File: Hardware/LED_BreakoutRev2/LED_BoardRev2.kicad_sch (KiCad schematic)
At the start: 33 parts, among them Q1 BSS214NW, Q2 BSS214NW, Q3 BSS214NW, Q4 BSS214NW, Q5 BSS214NW, Q6 BSS214NW

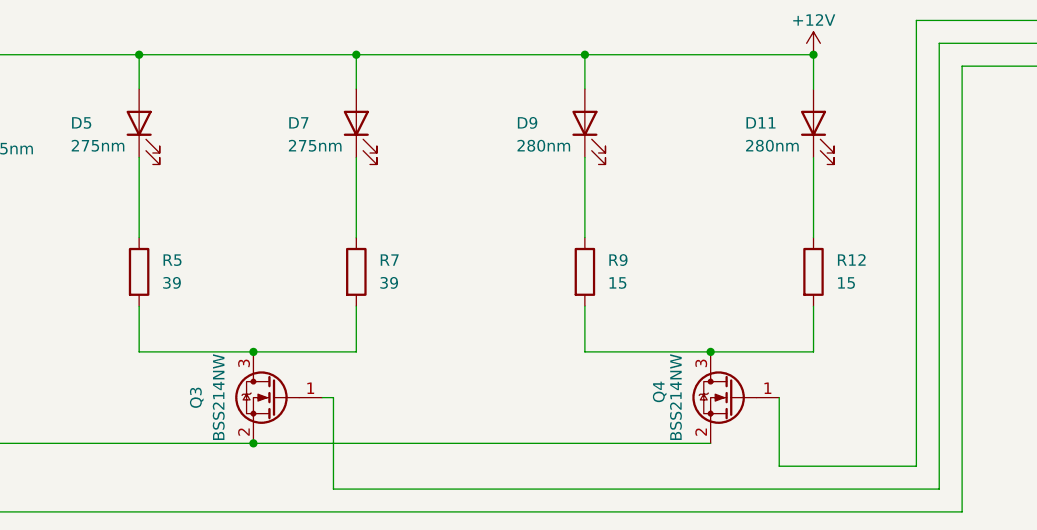
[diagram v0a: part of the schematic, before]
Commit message: Fixed resistor values
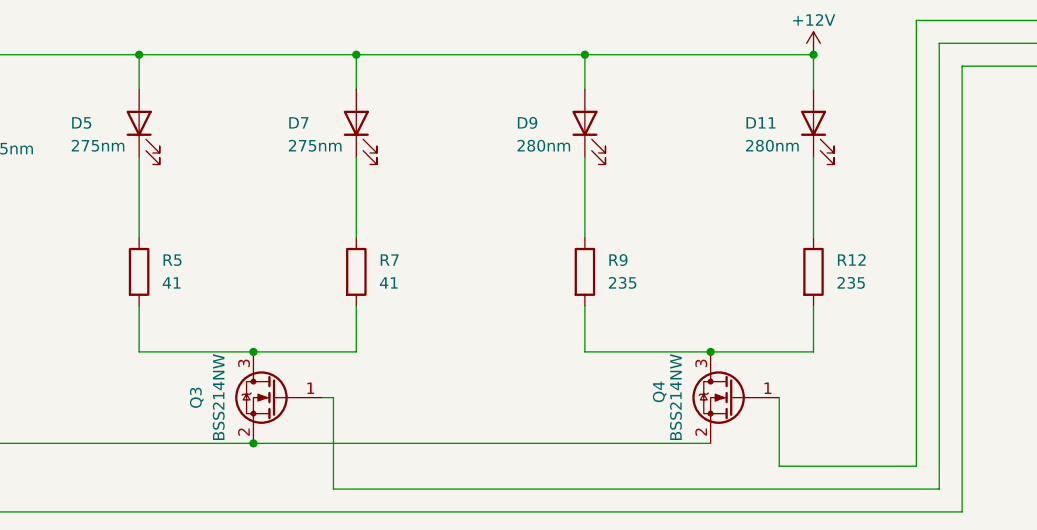
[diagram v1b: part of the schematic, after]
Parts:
- R12, R9: value 15 -> 235
- R5, R7: value 39 -> 41
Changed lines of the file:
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@@
       (effects (font (size 1.27 1.27)) (justify left))
     )
-    (property "Value" "15" (id 1) (at 201.93 110.4899 0)
+    (property "Value" "235" (id 1) (at 201.93 110.4899 0)
       (effects (font (size 1.27 1.27)) (justify left))
     )
@@
       (effects (font (size 1.27 1.27)) hide)
     )
-    (property "Datasheet" "https://www.digikey.com/en/products/detail/te-connectivity-passive-product/352215RFT/5244998" (id 3) (at 199.39 109.22 0)
+    (property "Datasheet" "https://www.mouser.com/ProductDetail/YAGEO/RT1206BRC07250RL?qs=sGAEpiMZZMtlubZbdhIBINSnPd898yDPjn3BpsSGDUg%3D" (id 3) (at 199.39 109.22 0)
       (effects (font (size 1.27 1.27)) hide)
     )
@@
       (effects (font (size 1.27 1.27)) (justify left))
     )
-    (property "Value" "39" (id 1) (at 151.13 110.4899 0)
+    (property "Value" "41" (id 1) (at 151.13 110.4899 0)
       (effects (font (size 1.27 1.27)) (justify left))
     )
@@
       (effects (font (size 1.27 1.27)) (justify left))
     )
-    (property "Value" "15" (id 1) (at 176.53 110.4899 0)
+    (property "Value" "235" (id 1) (at 176.53 110.4899 0)
       (effects (font (size 1.27 1.27)) (justify left))
     )
@@
       (effects (font (size 1.27 1.27)) hide)
     )
-    (property "Datasheet" "https://www.digikey.com/en/products/detail/te-connectivity-passive-product/352215RFT/5244998" (id 3) (at 173.99 109.22 0)
+    (property "Datasheet" "https://www.mouser.com/ProductDetail/YAGEO/RT1206BRC07250RL?qs=sGAEpiMZZMtlubZbdhIBINSnPd898yDPjn3BpsSGDUg%3D" (id 3) (at 173.99 109.22 0)
       (effects (font (size 1.27 1.27)) hide)
     )
@@
       (effects (font (size 1.27 1.27)) (justify left))
     )
-    (property "Value" "39" (id 1) (at 127 110.4899 0)
+    (property "Value" "41" (id 1) (at 127 110.4899 0)
       (effects (font (size 1.27 1.27)) (justify left))
     )
@@
     )
     (path "/93e48d0b-eba6-4854-bc8a-17e527f014a3"
-      (reference "R5") (unit 1) (value "39") (footprint "Resistor_SMD:R_2512_6332Metric_Pad1.40x3.35mm_HandSolder")
+      (reference "R5") (unit 1) (value "41") (footprint "Resistor_SMD:R_2512_6332Metric_Pad1.40x3.35mm_HandSolder")
     )
     (path "/d17db897-84e6-4022-9dc4-4eecd630bc5e"
@@
     )
     (path "/240d6f4d-65b2-4461-b47d-786ff4cb3d7c"
-      (reference "R7") (unit 1) (value "39") (footprint "Resistor_SMD:R_2512_6332Metric_Pad1.40x3.35mm_HandSolder")
+      (reference "R7") (unit 1) (value "41") (footprint "Resistor_SMD:R_2512_6332Metric_Pad1.40x3.35mm_HandSolder")
     )
     (path "/1e5baa22-f800-4ee7-823e-07c8c8a82f1b"
@@
     )
     (path "/4640cc32-5742-46fb-92d3-8c957470f387"
-      (reference "R9") (unit 1) (value "15") (footprint "Resistor_SMD:R_2512_6332Metric_Pad1.40x3.35mm_HandSolder")
+      (reference "R9") (unit 1) (value "235") (footprint "Resistor_SMD:R_2512_6332Metric_Pad1.40x3.35mm_HandSolder")
     )
     (path "/7d784730-35d8-402c-a5c8-e39754989647"
@@
     )
     (path "/1d427fac-f5cd-4da2-9ce4-13d315414bcf"
-      (reference "R12") (unit 1) (value "15") (footprint "Resistor_SMD:R_2512_6332Metric_Pad1.40x3.35mm_HandSolder")
+      (reference "R12") (unit 1) (value "235") (footprint "Resistor_SMD:R_2512_6332Metric_Pad1.40x3.35mm_HandSolder")
     )
     (path "/fc7a2316-8b3d-43bf-ad9b-b37462b729ed"

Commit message: Update datasheet
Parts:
- removed R10, R11, R13: 4, MRDT_Devices:Stupid 4 Ohm Resistor, symbol Device:R
- removed R12: 235, Resistor_SMD:R_2512_6332Metric_Pad1.40x3.35mm_HandSolder, symbol Device:R
- added R?: 16, MRDT_Devices:Stupid 4 Ohm Resistor, symbol Device:R
- added R?: 237, Resistor_SMD:R_2512_6332Metric_Pad1.40x3.35mm_HandSolder, symbol Device:R
- R1: value 250 -> 325
- R14: value 4 -> 16
- R4, R6, R8: value 150 -> 325
- R5, R7: value 41 -> 39
- R9: value 235 -> 237
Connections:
- net at D10.1 (K): now also R?.1
- net at D11.1 (K): now also R?.1
- net at Q4.3 (D), R9.2: now also R?.2
- net at D12.1 (K): now also R14.1
- net at Q5.3 (D), Q6.3 (D), R14.2: now also R?.2
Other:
- moved on the sheet: R14

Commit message: Concept LED layout
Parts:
- removed R14: 16, MRDT_Devices:Stupid 4 Ohm Resistor, symbol Device:R
- added R12: 16, Resistor_SMD:R_2512_6332Metric_Pad1.40x3.35mm_HandSolder, symbol Device:R
- R10: renamed from R?; footprint MRDT_Devices:Stupid 4 Ohm Resistor -> Resistor_SMD:R_2512_6332Metric_Pad1.40x3.35mm_HandSolder
- gave numbers to parts that had none: 1
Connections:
- net at Q5.3 (D), Q6.3 (D), R10.2: now also R12.2
- net at D12.1 (K): now also R12.1
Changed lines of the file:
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@@
   (symbol (lib_id "Device:R") (at 190.5 52.07 0) (unit 1)
     (in_bom yes) (on_board yes) (fields_autoplaced)
-    (property "Reference" "R?" (id 0) (at 193.04 50.7999 0)
+    (property "Reference" "R10" (id 0) (at 193.04 50.7999 0)
       (effects (font (size 1.27 1.27)) (justify left))
     )
@@
       (effects (font (size 1.27 1.27)) (justify left))
     )
-    (property "Footprint" "MRDT_Devices:Stupid 4 Ohm Resistor" (id 2) (at 188.722 52.07 90)
+    (property "Footprint" "Resistor_SMD:R_2512_6332Metric_Pad1.40x3.35mm_HandSolder" (id 2) (at 188.722 52.07 90)
       (effects (font (size 1.27 1.27)) hide)
     )
@@
     (pin "2")
   )
+  (symbol (lib_id "Device:R") (at 209.55 52.07 0) (unit 1)
+    (in_bom yes) (on_board yes) (fields_autoplaced)
+    (property "Reference" "R12" (id 0) (at 212.09 50.7999 0)
+      (effects (font (size 1.27 1.27)) (justify left))
+    )
+    (property "Value" "16" (id 1) (at 212.09 53.3399 0)
+      (effects (font (size 1.27 1.27)) (justify left))
+    )
+    (property "Footprint" "Resistor_SMD:R_2512_6332Metric_Pad1.40x3.35mm_HandSolder" (id 2) (at 207.772 52.07 90)
+      (effects (font (size 1.27 1.27)) hide)
+    )
+    (property "Datasheet" "https://www.digikey.com/en/products/detail/te-connectivity-passive-product/355016RFT/9927086?s=N4IgjCBcoExaBjKAzAhgGwM4FMA0IB7KAbRBgBYBOANgpAF18AHAFyhAGUWAnASwDsA5iAC%2B%2BAMzwQSSGix5CJcGHERGIVuy58ho-DAAMADgCsUmXJz4ikUmGoACAPIALALaYGzNpBABVfl4WJ2QAWWxUTABXbmw9EABaOGhpKB4ohRtSM3oRPKA" (id 3) (at 209.55 52.07 0)
+      (effects (font (size 1.27 1.27)) hide)
+    )
+    (pin "1")
+    (pin "2")
+  )
   (symbol (lib_id "Device:LED") (at 102.87 92.71 90) (unit 1)
     (in_bom yes) (on_board yes) (fields_autoplaced)
@@
     (pin "2")
   )
-  (symbol (lib_id "Device:R") (at 209.55 52.07 0) (unit 1)
-    (in_bom yes) (on_board yes) (fields_autoplaced)
-    (property "Reference" "R14" (id 0) (at 212.09 50.7999 0)
-      (effects (font (size 1.27 1.27)) (justify left))
-    )
-    (property "Value" "16" (id 1) (at 212.09 53.3399 0)
-      (effects (font (size 1.27 1.27)) (justify left))
-    )
-    (property "Footprint" "MRDT_Devices:Stupid 4 Ohm Resistor" (id 2) (at 207.772 52.07 90)
-      (effects (font (size 1.27 1.27)) hide)
-    )
-    (property "Datasheet" "https://www.digikey.com/en/products/detail/te-connectivity-passive-product/355016RFT/9927086?s=N4IgjCBcoExaBjKAzAhgGwM4FMA0IB7KAbRBgBYBOANgpAF18AHAFyhAGUWAnASwDsA5iAC%2B%2BAMzwQSSGix5CJcGHERGIVuy58ho-DAAMADgCsUmXJz4ikUmGoACAPIALALaYGzNpBABVfl4WJ2QAWWxUTABXbmw9EABaOGhpKB4ohRtSM3oRPKA" (id 3) (at 209.55 52.07 0)
-      (effects (font (size 1.27 1.27)) hide)
-    )
-    (pin "1")
-    (pin "2")
-  )
   (symbol (lib_id "Device:R") (at 134.62 50.8 0) (unit 1)
     (in_bom yes) (on_board yes) (fields_autoplaced)
@@
   (symbol (lib_id "Device:R") (at 199.39 109.22 0) (unit 1)
     (in_bom yes) (on_board yes) (fields_autoplaced)
-    (property "Reference" "R?" (id 0) (at 201.93 107.9499 0)
+    (property "Reference" "R11" (id 0) (at 201.93 107.9499 0)
       (effects (font (size 1.27 1.27)) (justify left))
     )
@@
       (reference "R9") (unit 1) (value "237") (footprint "Resistor_SMD:R_2512_6332Metric_Pad1.40x3.35mm_HandSolder")
     )
-    (path "/c5a7d028-8d34-4c0f-a3a9-dcd478aff00e"
-      (reference "R14") (unit 1) (value "16") (footprint "MRDT_Devices:Stupid 4 Ohm Resistor")
-    )
     (path "/2554a1ee-c9a5-4022-9b27-f04f246a3a90"
-      (reference "R?") (unit 1) (value "16") (footprint "MRDT_Devices:Stupid 4 Ohm Resistor")
+      (reference "R10") (unit 1) (value "16") (footprint "Resistor_SMD:R_2512_6332Metric_Pad1.40x3.35mm_HandSolder")
     )
     (path "/d92f54a0-29d1-4247-85fa-7317112c0582"
-      (reference "R?") (unit 1) (value "237") (footprint "Resistor_SMD:R_2512_6332Metric_Pad1.40x3.35mm_HandSolder")
-    )
-  )
+      (reference "R11") (unit 1) (value "237") (footprint "Resistor_SMD:R_2512_6332Metric_Pad1.40x3.35mm_HandSolder")
+    )
+    (path "/4e94a3e2-c33c-4c00-83d6-277a72b6be7a"
+      (reference "R12") (unit 1) (value "16") (footprint "Resistor_SMD:R_2512_6332Metric_Pad1.40x3.35mm_HandSolder")
+    )
+  )

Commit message: Still moving footprints
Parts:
- D5, D7: footprint MRDT_Devices:275nm LED -> Footprints:SU CULCN1.VC
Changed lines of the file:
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@@
-    (pin "2")
-  )
-  (symbol (lib_id "Device:LED") (at 148.59 92.71 90) (unit 1)
-    (in_bom yes) (on_board yes)
-    (property "Reference" "D7" (id 0) (at 140.97 92.71 90)
-      (effects (font (size 1.27 1.27)) (justify right))
-    )
-    (property "Value" "275nm" (id 1) (at 140.97 95.25 90)
-      (effects (font (size 1.27 1.27)) (justify right))
-    )
-    (property "Footprint" "MRDT_Devices:275nm LED" (id 2) (at 148.59 92.71 0)
-      (effects (font (size 1.27 1.27)) hide)
-    )
-    (property "Datasheet" "https://www.mouser.com/ProductDetail/ams-OSRAM/SU-CULCN1VC-GAGD-67-0-100-R18?qs=QNEnbhJQKvYzTEg60TYLDA%3D%3D&mgh=1&gclid=Cj0KCQjww4-hBhCtARIsAC9gR3Yx9EYuuzoX6Epv-96pbTp_j3rO-uPwrYGY7enRByVU-IZeXYdc4EkaAnjkEALw_wcB" (id 3) (at 148.59 92.71 0)
-      (effects (font (size 1.27 1.27)) hide)
-    )
-    (pin "1")
     (pin "2")
   )
@@
     (pin "1")
   )
+  (symbol (lib_id "Device:LED") (at 148.59 92.71 90) (unit 1)
+    (in_bom yes) (on_board yes)
+    (property "Reference" "D7" (id 0) (at 140.97 92.71 90)
+      (effects (font (size 1.27 1.27)) (justify right))
+    )
+    (property "Value" "275nm" (id 1) (at 140.97 95.25 90)
+      (effects (font (size 1.27 1.27)) (justify right))
+    )
+    (property "Footprint" "Footprints:SU CULCN1.VC" (id 2) (at 148.59 92.71 0)
+      (effects (font (size 1.27 1.27)) hide)
+    )
+    (property "Datasheet" "https://www.mouser.com/ProductDetail/ams-OSRAM/SU-CULCN1VC-GAGD-67-0-100-R18?qs=QNEnbhJQKvYzTEg60TYLDA%3D%3D&mgh=1&gclid=Cj0KCQjww4-hBhCtARIsAC9gR3Yx9EYuuzoX6Epv-96pbTp_j3rO-uPwrYGY7enRByVU-IZeXYdc4EkaAnjkEALw_wcB" (id 3) (at 148.59 92.71 0)
+      (effects (font (size 1.27 1.27)) hide)
+    )
+    (pin "1")
+    (pin "2")
+  )
   (symbol (lib_id "Device:LED") (at 124.46 92.71 90) (unit 1)
     (in_bom yes) (on_board yes)
@@
       (effects (font (size 1.27 1.27)) (justify right))
     )
-    (property "Footprint" "MRDT_Devices:275nm LED" (id 2) (at 124.46 92.71 0)
+    (property "Footprint" "Footprints:SU CULCN1.VC" (id 2) (at 124.46 92.71 0)
       (effects (font (size 1.27 1.27)) hide)
     )
@@
     )
     (path "/8b661577-1e9f-41b7-9774-6161b29c2028"
-      (reference "D5") (unit 1) (value "275nm") (footprint "MRDT_Devices:275nm LED")
+      (reference "D5") (unit 1) (value "275nm") (footprint "Footprints:SU CULCN1.VC")
     )
     (path "/dcb7ef33-50a6-417f-bcae-0dd5e0a1223d"
       (reference "D6") (unit 1) (value "310nm") (footprint "MRDT_Devices:310nm")
     )
-    (path "/1be29f99-8e79-49c2-8e00-bc12d0fc7593"
-      (reference "D7") (unit 1) (value "275nm") (footprint "MRDT_Devices:275nm LED")
+    (path "/89673091-85ee-47dd-91b8-23d167cba003"
+      (reference "D7") (unit 1) (value "275nm") (footprint "Footprints:SU CULCN1.VC")
     )
     (path "/ee50deb6-59ae-401b-9ef3-14286fd15a37"

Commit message: Changing layout
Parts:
- D10, D12: footprint MRDT_Devices:365nm LED -> Footprints:LZ1-00UV0R
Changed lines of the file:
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@@
       (effects (font (size 1.27 1.27)) (justify right))
     )
-    (property "Footprint" "MRDT_Devices:365nm LED" (id 2) (at 190.5 39.37 0)
+    (property "Footprint" "Footprints:LZ1-00UV0R" (id 2) (at 190.5 39.37 0)
       (effects (font (size 1.27 1.27)) hide)
     )
@@
     )
     (property "Datasheet" "https://www.mouser.com/ProductDetail/Vishay-Semiconductors/VLMU35CL20-275-120?qs=sPbYRqrBIVnwsuA%2FMQjGuQ%3D%3D" (id 3) (at 199.39 92.71 0)
-      (effects (font (size 1.27 1.27)) hide)
-    )
-    (pin "1")
-    (pin "2")
-  )
-  (symbol (lib_id "Device:LED") (at 209.55 39.37 90) (unit 1)
-    (in_bom yes) (on_board yes)
-    (property "Reference" "D12" (id 0) (at 201.93 39.37 90)
-      (effects (font (size 1.27 1.27)) (justify right))
-    )
-    (property "Value" "365nm" (id 1) (at 201.93 41.91 90)
-      (effects (font (size 1.27 1.27)) (justify right))
-    )
-    (property "Footprint" "MRDT_Devices:365nm LED" (id 2) (at 209.55 39.37 0)
-      (effects (font (size 1.27 1.27)) hide)
-    )
-    (property "Datasheet" "https://www.digikey.com/en/products/detail/osram-sylvania-inc./LZ1-00UV0R-0000/10441131?utm_adgroup=Infrared%2C%20UV%2C%20Visible%20Emitters&utm_source=google&utm_medium=cpc&utm_campaign=Shopping_Product_Optoelectronics_NEW&utm_term=&utm_content=Infrared%2C%20UV%2C%20Visible%20Emitters&gclid=Cj0KCQjww4-hBhCtARIsAC9gR3Zin1EjcHelMRn99sYYosUo0ZWMWYvGeo7J6bgWsph-cu9-1cPf-0saAlrnEALw_wcB" (id 3) (at 209.55 39.37 0)
       (effects (font (size 1.27 1.27)) hide)
     )
@@
     (pin "1")
   )
+  (symbol (lib_id "Device:LED") (at 209.55 39.37 90) (unit 1)
+    (in_bom yes) (on_board yes)
+    (property "Reference" "D12" (id 0) (at 201.93 39.37 90)
+      (effects (font (size 1.27 1.27)) (justify right))
+    )
+    (property "Value" "365nm" (id 1) (at 201.93 41.91 90)
+      (effects (font (size 1.27 1.27)) (justify right))
+    )
+    (property "Footprint" "Footprints:LZ1-00UV0R" (id 2) (at 209.55 39.37 0)
+      (effects (font (size 1.27 1.27)) hide)
+    )
+    (property "Datasheet" "https://www.digikey.com/en/products/detail/osram-sylvania-inc./LZ1-00UV0R-0000/10441131?utm_adgroup=Infrared%2C%20UV%2C%20Visible%20Emitters&utm_source=google&utm_medium=cpc&utm_campaign=Shopping_Product_Optoelectronics_NEW&utm_term=&utm_content=Infrared%2C%20UV%2C%20Visible%20Emitters&gclid=Cj0KCQjww4-hBhCtARIsAC9gR3Zin1EjcHelMRn99sYYosUo0ZWMWYvGeo7J6bgWsph-cu9-1cPf-0saAlrnEALw_wcB" (id 3) (at 209.55 39.37 0)
+      (effects (font (size 1.27 1.27)) hide)
+    )
+    (pin "1")
+    (pin "2")
+  )
   (symbol (lib_id "power:+12V") (at 199.39 85.09 0) (unit 1)
     (in_bom yes) (on_board yes)
@@
     )
     (path "/19a29233-f3ee-4a69-a817-a5602e2e22f0"
-      (reference "D10") (unit 1) (value "365nm") (footprint "MRDT_Devices:365nm LED")
+      (reference "D10") (unit 1) (value "365nm") (footprint "Footprints:LZ1-00UV0R")
     )
     (path "/258dfcd1-148d-4d20-a98b-cb4692e2a49b"
       (reference "D11") (unit 1) (value "280nm") (footprint "MRDT_Devices:280nm")
     )
-    (path "/34f06e75-2491-4222-bc96-b30568212ad1"
-      (reference "D12") (unit 1) (value "365nm") (footprint "MRDT_Devices:365nm LED")
+    (path "/634063c4-cc7e-48f7-a28d-710f51cd0425"
+      (reference "D12") (unit 1) (value "365nm") (footprint "Footprints:LZ1-00UV0R")
     )
     (path "/03b35fcf-5331-435b-846e-4278c0f5f6f9"

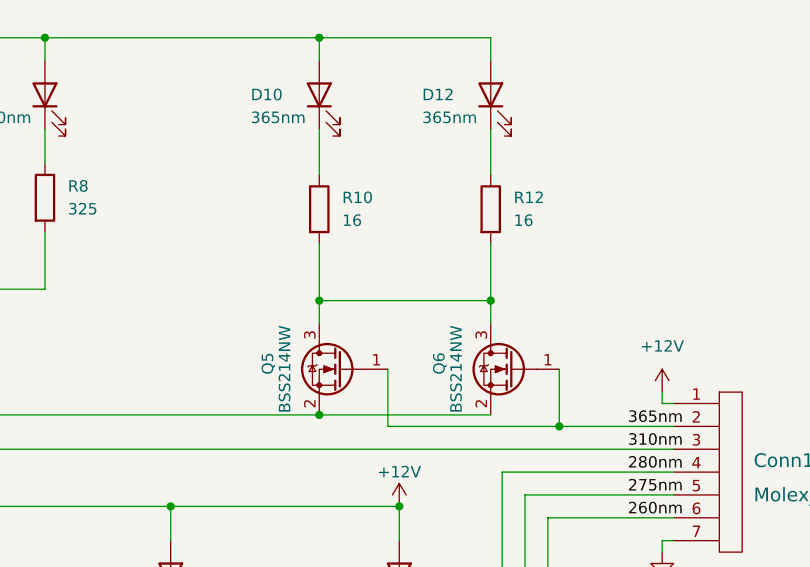
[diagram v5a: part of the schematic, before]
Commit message: Editing LED placement
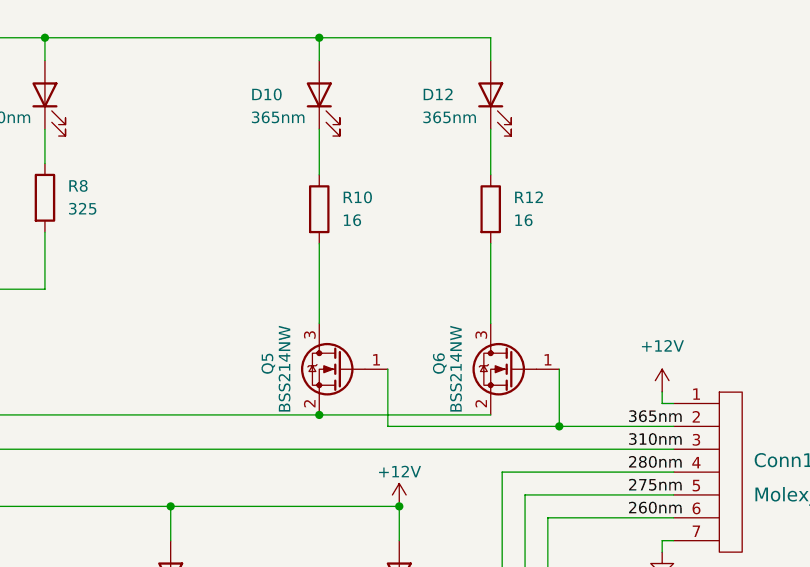
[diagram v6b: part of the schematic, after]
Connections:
- net at Q5.3 (D), R10.2: no longer Q6.3 (D), R12.2
- new net: Q6.3 (D), R12.2
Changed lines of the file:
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@@
 (kicad_sch (version 20211123) (generator eeschema)
   (paper "A4")
-  (junction (at 190.5 62.23) (diameter 0) (color 0 0 0 0)
-  )
   (junction (at 134.62 60.96) (diameter 0) (color 0 0 0 0)
   )
@@
   (junction (at 81.28 33.02) (diameter 0) (color 0 0 0 0)
   )
-  (junction (at 209.55 62.23) (diameter 0) (color 0 0 0 0)
-  )
   (junction (at 102.87 85.09) (diameter 0) (color 0 0 0 0)
   )
@@
     (stroke (width 0) (type default) (color 0 0 0 0))
   )
-  (wire (pts (xy 190.5 62.23) (xy 209.55 62.23))
-    (stroke (width 0) (type default) (color 0 0 0 0))
-  )
   (wire (pts (xy 217.17 76.2) (xy 229.87 76.2))
     (stroke (width 0) (type default) (color 0 0 0 0))
@@
     (stroke (width 0) (type default) (color 0 0 0 0))
   )
-  (wire (pts (xy 209.55 62.23) (xy 209.55 64.77))
-    (stroke (width 0) (type default) (color 0 0 0 0))
-  )
   (wire (pts (xy 134.62 54.61) (xy 134.62 60.96))
     (stroke (width 0) (type default) (color 0 0 0 0))
@@
     (stroke (width 0) (type default) (color 0 0 0 0))
   )
-  (wire (pts (xy 209.55 55.88) (xy 209.55 62.23))
+  (wire (pts (xy 209.55 55.88) (xy 209.55 64.77))
     (stroke (width 0) (type default) (color 0 0 0 0))
   )
@@
     (stroke (width 0) (type default) (color 0 0 0 0))
   )
-  (wire (pts (xy 190.5 55.88) (xy 190.5 62.23))
-    (stroke (width 0) (type default) (color 0 0 0 0))
-  )
   (wire (pts (xy 102.87 96.52) (xy 102.87 105.41))
     (stroke (width 0) (type default) (color 0 0 0 0))
@@
     (stroke (width 0) (type default) (color 0 0 0 0))
   )
-  (wire (pts (xy 190.5 62.23) (xy 190.5 64.77))
-    (stroke (width 0) (type default) (color 0 0 0 0))
-  )
+  (wire (pts (xy 190.5 55.88) (xy 190.5 64.77))
+    (stroke (width 0) (type default) (color 0 0 0 0))
+  )

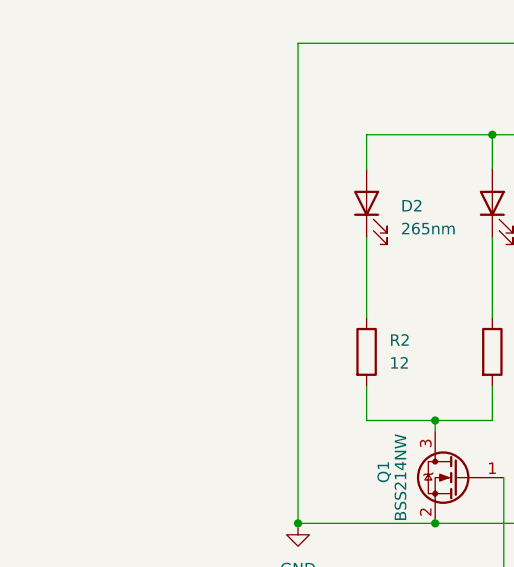
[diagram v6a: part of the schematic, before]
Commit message: Moving MOSFTETs over to instruments board
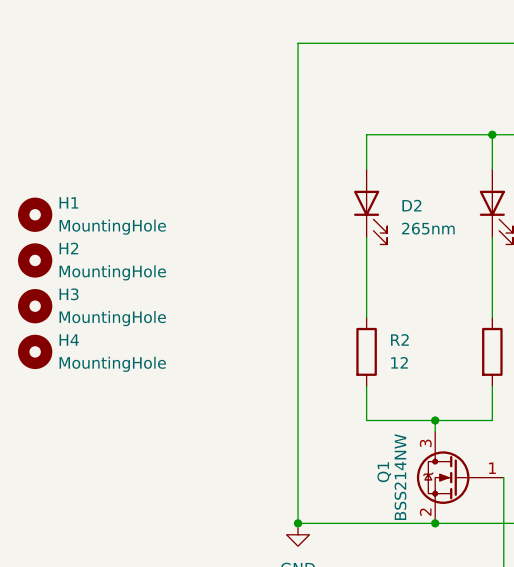
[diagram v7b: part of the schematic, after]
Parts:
- added H1, H2, H3, H4: MountingHole, MRDT_Drill_Holes:4_40_Hole_Corner, symbol Mechanical:MountingHole
- D1, D4, D6, D8: footprint MRDT_Devices:310nm -> Footprints:1414_3535_Metric
- D11, D9: footprint MRDT_Devices:280nm -> Footprints:VLMU35CL2.-275-120
- D2, D3: footprint KL265-50W-SM-WD Footprint:3535 -> Footprints:1414_3535_Metric
